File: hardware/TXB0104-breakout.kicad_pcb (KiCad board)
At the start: 2 copper layers, 16.8 x 19.1 mm, 6 parts, among them J1 Conn_01x07_Male, J2 Conn_01x07_Male, U1 TXB0104D

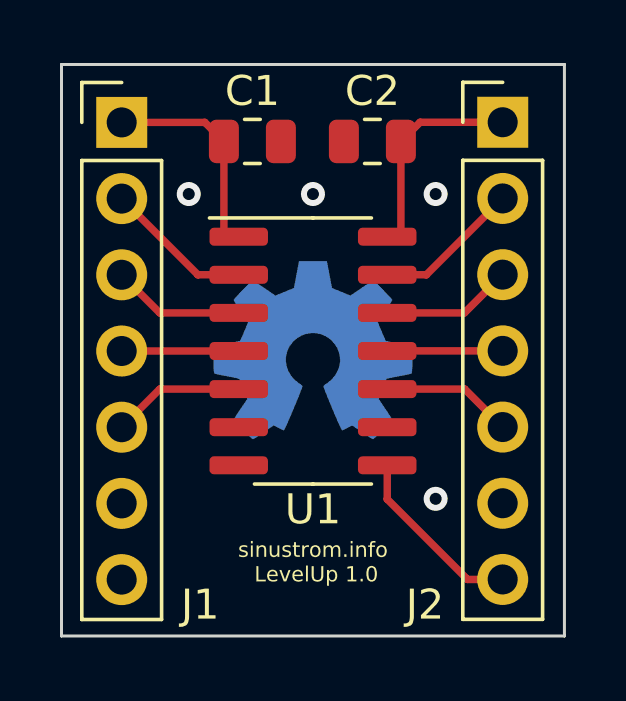
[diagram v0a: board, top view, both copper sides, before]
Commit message: Update board
- add pull down resistor to output enable pin to ensure off state during
  power on
- remove extra gound planes from the signal layer to reduce potential RF
  emissions from the board
- fix bottom silk screen
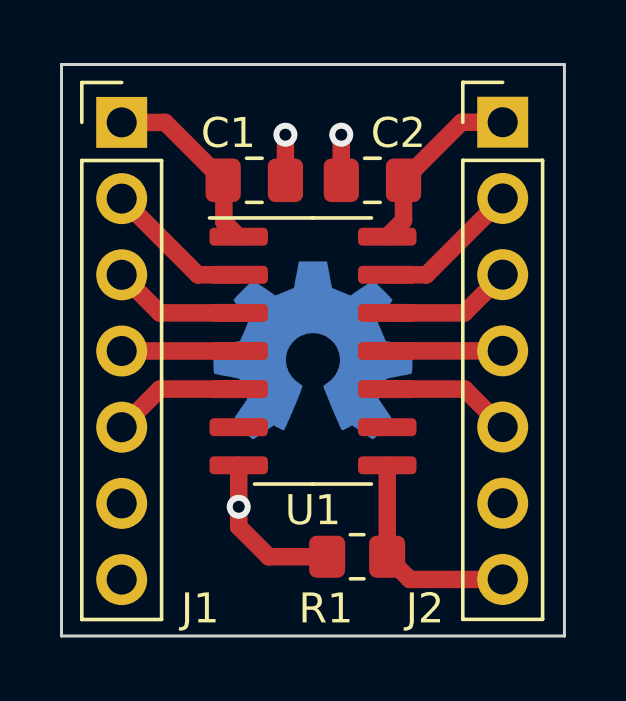
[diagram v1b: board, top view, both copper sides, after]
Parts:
- added R1: 10k, Resistor_SMD:R_0805_2012Metric_Pad1.20x1.40mm_HandSolder, F.Cu at (109.2, 72.7)
- C1, C2: footprint Capacitor_SMD:C_0805_2012Metric -> Capacitor_SMD:C_0805_2012Metric_Pad1.18x1.45mm_HandSolder
- moved C1 1.30 mm to (105.7, 60.2)
- moved C2 1.30 mm to (109.7, 60.2)
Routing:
- net GND: track 0.00 -> 8.45 mm, vias 4 -> 3
- net /OE: track 6.09 -> 7.21 mm
- net +5V: track 7.27 -> 6.21 mm
- removed copper zone on F.Cu, net GND
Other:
- board text added: "TXB0104D sinustrom.info"
- board text added: "X X"
- board text removed: "NC NC"
- board text removed: "TXB0104"
- board text removed: "sinustrom.info LevelUp 1.0"

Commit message: Fine tune PCB
- Move ground vias for the bypass capacitors closer to power lines to
  reduce loop size
- Update bottom silk screen text arrangement for more symmetry
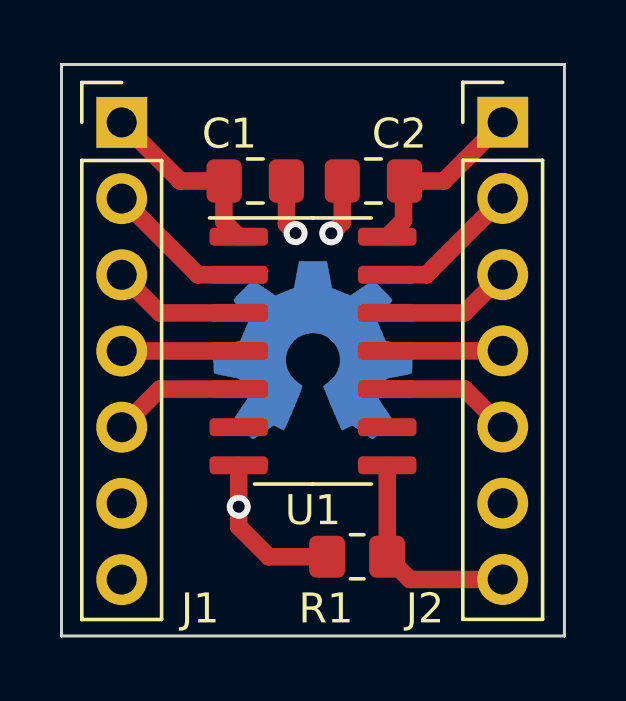
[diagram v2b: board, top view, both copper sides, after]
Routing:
- net GND: track 8.45 -> 9.17 mm
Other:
- board text added: "TXB0104D"
- board text added: "sinustrom.info"
- board text removed: "TXB0104D sinustrom.info"
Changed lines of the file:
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@@
     (title "TXB0104-breakout")
     (date "2022-01-22")
-    (rev "1.1")
+    (rev "1.2")
     (company "sinustrom.info")
     (comment 1 "https://github.com/zpuskas/TXB0104-breakout")
@@
   (net 16 "unconnected-(U1-Pad9)")
   (footprint "Capacitor_SMD:C_0805_2012Metric_Pad1.18x1.45mm_HandSolder" (layer "F.Cu")
-    (at 105.7402 60.198)
+    (at 105.77322 60.22086)
     (descr "Capacitor SMD 0805 (2012 Metric), square (rectangular) end terminal, IPC_7351 nominal with elongated pad for handsoldering. (Body size source: IPC-SM-782 page 76, https://www.pcb-3d.com/wordpress/wp-content/uploads/ipc-sm-782a_amendment_1_and_2.pdf, https://docs.google.com/spreadsheets/d/1BsfQQcO9C6DZCsRaXUlFlo91Tg2WpOkGARC1WS5S8t0/edit?usp=sharing), generated with kicad-footprint-generator")
     (tags "capacitor handsolder")
@@
   )
   (footprint "Capacitor_SMD:C_0805_2012Metric_Pad1.18x1.45mm_HandSolder" (layer "F.Cu")
-    (at 109.6772 60.198 180)
+    (at 109.71022 60.22086 180)
     (descr "Capacitor SMD 0805 (2012 Metric), square (rectangular) end terminal, IPC_7351 nominal with elongated pad for handsoldering. (Body size source: IPC-SM-782 page 76, https://www.pcb-3d.com/wordpress/wp-content/uploads/ipc-sm-782a_amendment_1_and_2.pdf, https://docs.google.com/spreadsheets/d/1BsfQQcO9C6DZCsRaXUlFlo91Tg2WpOkGARC1WS5S8t0/edit?usp=sharing), generated with kicad-footprint-generator")
     (tags "capacitor handsolder")
@@
     (effects (font (size 1 1) (thickness 0.15)) (justify mirror))
   )
+  (gr_text "TXB0104D" (at 109.07522 65.8876 270) (layer "B.SilkS")
+    (effects (font (size 1 1) (thickness 0.15)) (justify mirror))
+  )
   (gr_text "X          X" (at 107.696 70.9626) (layer "B.SilkS")
     (effects (font (size 1 1) (thickness 0.15)) (justify mirror))
@@
     (effects (font (size 1 1) (thickness 0.15)) (justify mirror))
   )
-  (gr_text "  TXB0104D\nsinustrom.info" (at 107.696 65.8876 270) (layer "B.SilkS")
+  (gr_text "sinustrom.info" (at 106.2228 65.8876 270) (layer "B.SilkS")
     (effects (font (size 1 1) (thickness 0.15)) (justify mirror))
   )
@@
     (effects (font (size 1 1) (thickness 0.15)) (justify mirror))
   )
-  (segment (start 104.7027 60.198) (end 104.6988 60.198) (width 0.5842) (layer "F.Cu") (net 1))
+  (segment (start 104.728112 61.584688) (end 104.728112 60.228468) (width 0.5842) (layer "F.Cu") (net 1))
+  (segment (start 104.73572 60.22086) (end 103.27386 60.22086) (width 0.5842) (layer "F.Cu") (net 1))
+  (segment (start 103.27386 60.22086) (end 101.3206 58.2676) (width 0.5842) (layer "F.Cu") (net 1))
+  (segment (start 105.220999 62.0776) (end 104.728112 61.584688) (width 0.5842) (layer "F.Cu") (net 1))
   (segment (start 104.8004 62.0776) (end 104.7272 62.0044) (width 0.25) (layer "F.Cu") (net 1))
   (segment (start 105.221 62.0776) (end 104.8004 62.0776) (width 0.25) (layer "F.Cu") (net 1))
-  (segment (start 104.728112 61.584688) (end 105.220999 62.0776) (width 0.5842) (layer "F.Cu") (net 1))
-  (segment (start 104.6988 60.198) (end 102.7684 58.2676) (width 0.5842) (layer "F.Cu") (net 1))
-  (segment (start 104.728112 60.223412) (end 104.7027 60.198) (width 0.5842) (layer "F.Cu") (net 1))
-  (segment (start 104.728112 61.584688) (end 104.728112 60.223412) (width 0.5842) (layer "F.Cu") (net 1))
-  (segment (start 102.7684 58.2676) (end 101.3206 58.2676) (width 0.5842) (layer "F.Cu") (net 1))
+  (segment (start 104.728112 60.228468) (end 104.73572 60.22086) (width 0.5842) (layer "F.Cu") (net 1))
   (segment (start 105.220999 71.080401) (end 105.220999 71.743799) (width 0.5842) (layer "F.Cu") (net 2))
-  (segment (start 106.777688 60.198) (end 106.777688 58.677912) (width 0.5842) (layer "F.Cu") (net 2))
   (segment (start 106.2228 72.7456) (end 108.1692 72.7456) (width 0.5842) (layer "F.Cu") (net 2))
+  (segment (start 106.810708 61.652048) (end 107.11688 61.95822) (width 0.5842) (layer "F.Cu") (net 2))
   (segment (start 105.220999 71.080401) (end 105.221 69.6976) (width 0.5842) (layer "F.Cu") (net 2))
-  (segment (start 108.639712 60.198) (end 108.639712 58.677912) (width 0.5842) (layer "F.Cu") (net 2))
+  (segment (start 108.672732 60.22086) (end 108.672732 61.598708) (width 0.5842) (layer "F.Cu") (net 2))
+  (segment (start 106.810708 60.22086) (end 106.810708 61.652048) (width 0.5842) (layer "F.Cu") (net 2))
+  (segment (start 108.672732 61.598708) (end 108.3056 61.96584) (width 0.5842) (layer "F.Cu") (net 2))
   (segment (start 105.220999 71.743799) (end 106.2228 72.7456) (width 0.5842) (layer "F.Cu") (net 2))
-  (via (at 108.639712 58.677912) (size 0.8) (drill 0.4) (layers "F.Cu" "B.Cu") (net 2))
+  (via (at 108.3056 61.96584) (size 0.8) (drill 0.4) (layers "F.Cu" "B.Cu") (net 2))
   (via (at 105.220999 71.080401) (size 0.8) (drill 0.4) (layers "F.Cu" "B.Cu") (net 2))
-  (via (at 106.777688 58.677912) (size 0.8) (drill 0.4) (layers "F.Cu" "B.Cu") (net 2))
-  (segment (start 110.714688 60.198) (end 112.650092 58.262596) (width 0.5842) (layer "F.Cu") (net 3))
-  (segment (start 112.650092 58.262596) (end 114.0206 58.262596) (width 0.5842) (layer "F.Cu") (net 3))
-  (segment (start 110.714688 60.198) (end 110.714688 61.533888) (width 0.5842) (layer "F.Cu") (net 3))
-  (segment (start 110.714688 61.533888) (end 110.171001 62.0776) (width 0.5842) (layer "F.Cu") (net 3))
+  (via (at 107.11688 61.95822) (size 0.8) (drill 0.4) (layers "F.Cu" "B.Cu") (net 2))
+  (segment (start 112.06234 60.22086) (end 114.0206 58.2626) (width 0.5842) (layer "F.Cu") (net 3))
+  (segment (start 110.74772 60.22086) (end 112.06234 60.22086) (width 0.5842) (layer "F.Cu") (net 3))
+  (segment (start 110.714688 61.533888) (end 110.714688 60.253892) (width 0.5842) (layer "F.Cu") (net 3))
+  (segment (start 110.171001 62.0776) (end 110.714688 61.533888) (width 0.5842) (layer "F.Cu") (net 3))
+  (segment (start 110.714688 60.253892) (end 110.74772 60.22086) (width 0.5842) (layer "F.Cu") (net 3))
   (segment (start 103.8606 63.3476) (end 101.3206 60.8076) (width 0.5842) (layer "F.Cu") (net 4))
   (segment (start 105.220999 63.3476) (end 103.8606 63.3476) (width 0.5842) (layer "F.Cu") (net 4))
